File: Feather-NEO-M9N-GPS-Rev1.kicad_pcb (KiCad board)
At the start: 2 copper layers, 50.8 x 22.9 mm, 51 parts, among them IC1 PRTR5V0U2F,115, J6 USB_B_Micro, U1 NEO-M9N, U2 AP2112K-3.3

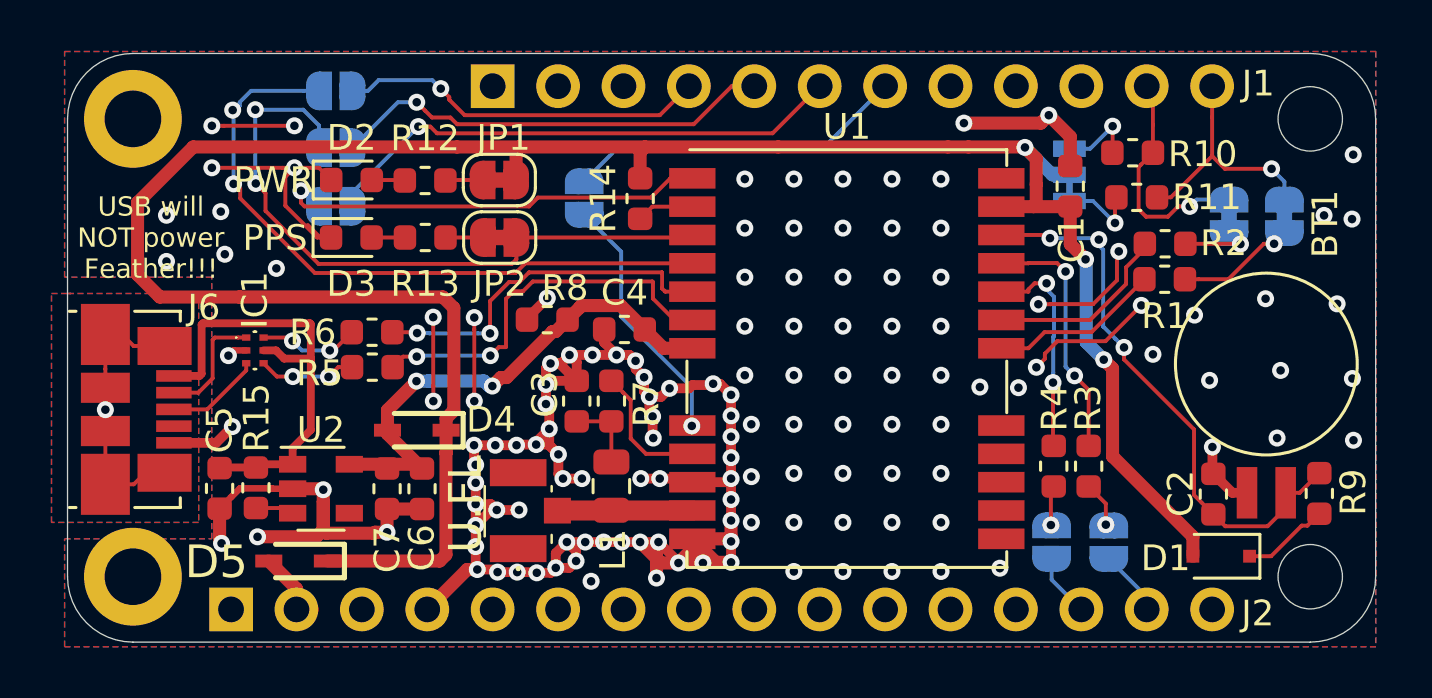
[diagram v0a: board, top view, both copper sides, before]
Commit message: Rev2!
Rev2 includes proper USB implementation, some small trace fixes, and power regulation
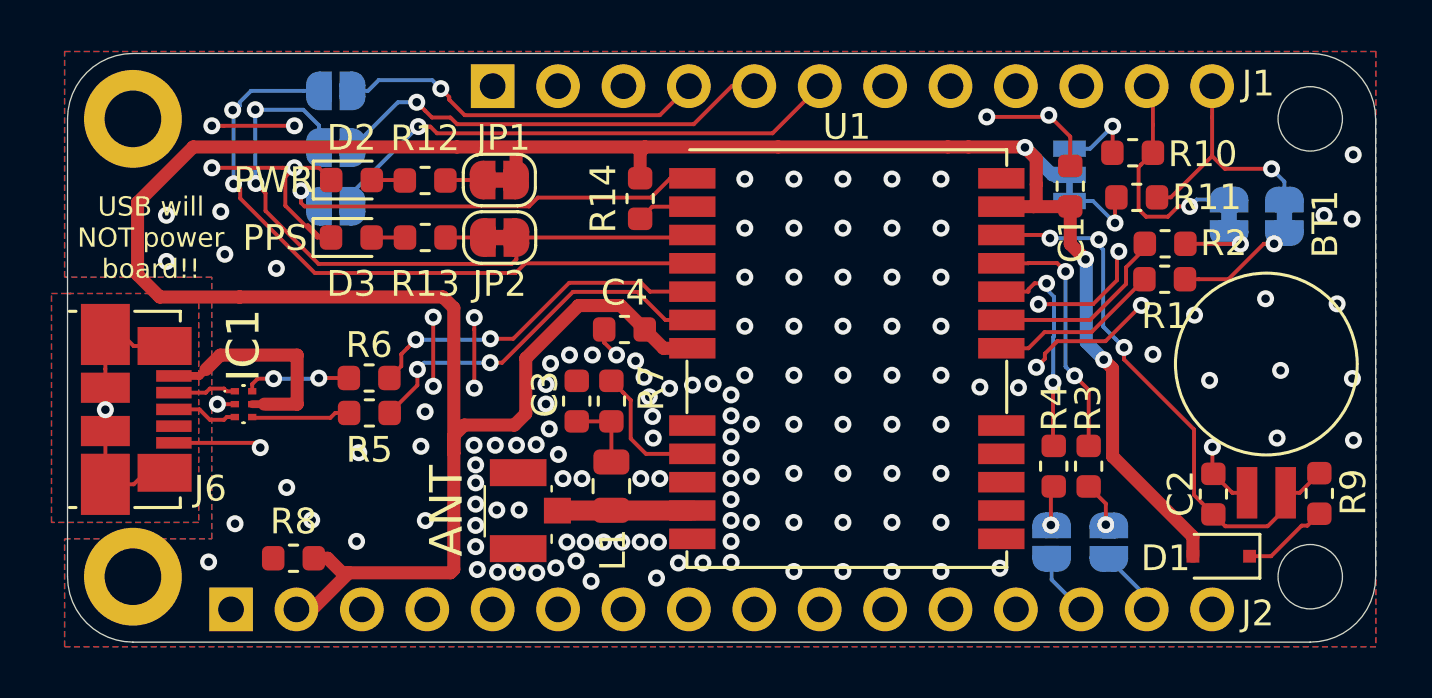
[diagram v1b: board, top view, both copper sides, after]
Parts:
- removed C5, C6: 10uF, Capacitor_SMD:C_0603_1608Metric
- removed C7: 1uF, Capacitor_SMD:C_0603_1608Metric
- removed D4, D5: BAT60AE6327HTSA1, SamacSys_Parts:SOD2513X110N
- removed JP5: ~RESET_GPS, Jumper:SolderJumper-2_P1.3mm_Open_RoundedPad1.0x1.5mm
- removed R15: 100k, Resistor_SMD:R_0603_1608Metric
- removed U2: AP2112K-3.3, Package_TO_SOT_SMD:SOT-23-5
- ANT1: value U.FL -> ANT
- moved R8 13.5 mm to (137.4, 94.1)
- moved IC1 2.13 mm to (135.5, 88.1)
- moved R6 1.78 mm to (140.4, 87.1)
- moved R5 1.78 mm to (140.4, 88.5)
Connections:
- net +5V renamed Net-(IC1-Pad5)
- C4 pad 2: /VDD_USB -> +3V3
- J2 pad 2: Net-(D5-Pad2) -> +3V3
- R8 pad 2: /VDD_USB -> +3V3
- U1 pad 7: /VDD_USB -> +3V3
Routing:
- net GND: track 127.7 -> 41.0 mm, vias 141 -> 146
- net /VDD_USB: track 20.1 -> 0.00 mm, vias 2 -> 0
- net +3V3: track 91.0 -> 109.0 mm
- net /10`: track 13.2 -> 0.00 mm
- net /~RESET_GPS: track 9.93 -> 0.00 mm, vias 1 -> 0
- net Net-(IC1-Pad5): track 17.9 -> 8.77 mm
- net Net-(D5-Pad2): track 2.93 -> 0.00 mm
- net Net-(IC1-Pad1): track 4.58 -> 2.48 mm
- net Net-(R15-Pad2): track 1.51 -> 0.00 mm
- net Net-(IC1-Pad3): track 3.71 -> 2.58 mm
- net Net-(R5-Pad1): track 15.1 -> 14.5 mm
- net /D+: track 3.81 -> 3.85 mm, vias 2 -> 0
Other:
- board text added: "Rev1 ABW 12/26/19"
- board text added: "USB will NOT power board!!"
- board text removed: "10"
- board text removed: "Rev2 ABW 1/6/20"
- board text removed: "USB will NOT power Feather!!!"
